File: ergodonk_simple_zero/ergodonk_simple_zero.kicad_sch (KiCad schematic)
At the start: 146 parts, among them J2 4PIN, Q1 TIP120, SW0 SW_PUSH_LED, SW08_RH10 SW_PUSH_LED, SW1 SW_PUSH_LED, SW10 SW_PUSH_LED, SW11 SW_PUSH_LED, SW12 SW_PUSH_LED, SW13 SW_PUSH_LED, SW14 SW_PUSH_LED, SW15 SW_PUSH_LED, SW16 SW_PUSH_LED, SW17 SW_PUSH_LED, SW18_RH10 SW_PUSH_LED, SW2 SW_PUSH_LED, SW20 SW_PUSH_LED, SW21 SW_PUSH_LED, SW22 SW_PUSH_LED, SW23 SW_PUSH_LED, SW24 SW_PUSH_LED, SW25 SW_PUSH_LED, SW26 SW_PUSH_LED, SW27 SW_PUSH_LED, SW28_RH10 SW_PUSH_LED, SW3 SW_PUSH_LED, SW30 SW_PUSH_LED, SW31 SW_PUSH_LED, SW32 SW_PUSH_LED, SW33 SW_PUSH_LED, SW34 SW_PUSH_LED, SW35 SW_PUSH_LED, SW36 SW_PUSH_LED, SW37 SW_PUSH_LED, SW38_RH10 SW_PUSH_LED, SW4 SW_PUSH_LED, SW40 SW_PUSH_LED, SW42 SW_PUSH_LED, SW43 SW_PUSH_LED, SW44 SW_PUSH_LED, SW45 SW_PUSH_LED, SW46 SW_PUSH_LED, SW47 SW_PUSH_LED, SW48_RH10 SW_PUSH_LED, SW5 SW_PUSH_LED, SW50 SW_PUSH_LED, SW51 SW_PUSH_LED, SW52 SW_PUSH_LED, SW53 SW_PUSH_LED, SW54 SW_PUSH_LED, SW55 SW_PUSH_LED, SW56 SW_PUSH_LED, SW57 SW_PUSH_LED, SW58 SW_PUSH_LED, SW6 SW_PUSH_LED, SW7 SW_PUSH_LED

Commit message: ergodonk simple zero checkpoint before choc MX switch swap
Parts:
- D_SOL_1: footprint ergodonk_simple:MUR340S_IN4001_TH_HYBRID -> Ergodonk_simple_zero:MUR340S_IN4001_TH_HYBRID
- H1, H10, H2, H3, H4, H5, H6, H7, H8, H9: footprint ergodonk_simple:Hole from sofle for M2 posts gold rimmer -> Ergodonk_simple_zero:Hole from sofle for M2 posts gold rimmer
- H11, H12, H13, H14, H15, H16, H17, H18, H19, H20, H21, H22, H23, H24, H25: footprint ergodonk_simple:M2_Hole_fancy_for_bolt-on-plate -> Ergodonk_simple_zero:M2_Hole_fancy_for_bolt-on-plate
- Q1: footprint ergodonk_simple:TO-220-3_Horizontal_TabDown -> Ergodonk_simple_zero:TO-220-3_Horizontal_TabDown
- SW0, SW1, SW10, SW11, SW12, SW13, SW14, SW16, SW17, SW2, SW20, SW21, SW22, SW23, SW24, SW25, SW26, SW3, SW30, SW31, SW32, SW33, SW34, SW35, SW36, SW4, SW40, SW42, SW43, SW44, SW45, SW46, SW5, SW50, SW51, SW52, SW53, SW54, SW55, SW56, SW57, SW58, SW6, SW7: footprint ergodonk_simple:Cherry_MX_DS_Hotswap_1U_sofle3b v3 -> Ergodonk_simple_zero:Cherry_MX_DS_Hotswap_1U_sofle3b v3
- SW08_RH10: footprint ergodonk_simple:V2_CherryMX_DoubleSided_Hotswap_miniE_2u_RH_ONLY -> Ergodonk_simple_zero:V2_CherryMX_DoubleSided_Hotswap_miniE_2u_RH_ONLY
- SW15: footprint kbd:CherryMX_Choc_Hotswap -> Ergodonk_simple_zero:CherryMX_Choc_Hotswap_ergodonk_simple_zero_56
- SW18_RH10, SW38_RH10: footprint ergodonk_simple:Cherry_MX_DS_Hotswap_1U_oneside -> Ergodonk_simple_zero:Cherry_MX_DS_Hotswap_1U_oneside
- SW27: footprint ergodonk_simple:V2_CherryMX_DoubleSided_Hotswap_miniE_1.5u_LH_1u_RH -> Ergodonk_simple_zero:V2_CherryMX_DoubleSided_Hotswap_miniE_1.5u_LH_1u_RH
- SW28_RH10: footprint ergodonk_simple:V2_CherryMX_DoubleSided_Hotswap_miniE_1.5u_RH_ONLY -> Ergodonk_simple_zero:V2_CherryMX_DoubleSided_Hotswap_miniE_1.5u_RH_ONLY
- SW37: footprint ergodonk_simple:V2_CherryMX_DoubleSided_Hotswap_miniE_1.75u_LH_1u_RH -> Ergodonk_simple_zero:V2_CherryMX_DoubleSided_Hotswap_miniE_1.75u_LH_1u_RH
- SW47: footprint ergodonk_simple:V2_CherryMX_DoubleSided_Hotswap_miniE_2.25u_LH_2.75u_RH -> Ergodonk_simple_zero:V2_CherryMX_DoubleSided_Hotswap_miniE_2.25u_LH_2.75u_RH
- SW48_RH10: footprint ergodonk_simple:V2_CherryMX_DoubleSided_Hotswap_miniE_2.25u_RH_ONLY -> Ergodonk_simple_zero:V2_CherryMX_DoubleSided_Hotswap_miniE_2.25u_RH_ONLY
- SWLH_ROT1: footprint ergodonk_simple:RotaryEncoder_EC11_ergodonk_variant -> Ergodonk_simple_zero:RotaryEncoder_EC11_ergodonk_variant

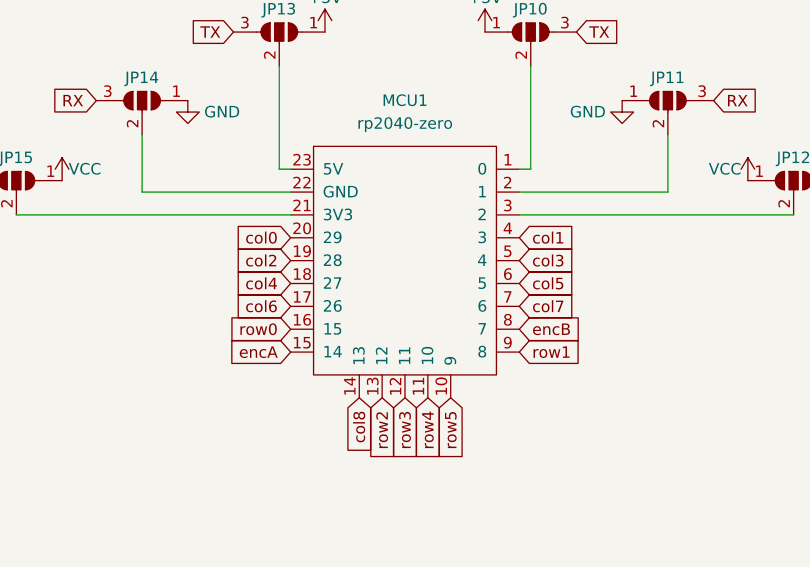
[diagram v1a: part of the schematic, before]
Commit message: Added choc support for ergodonk simple zero
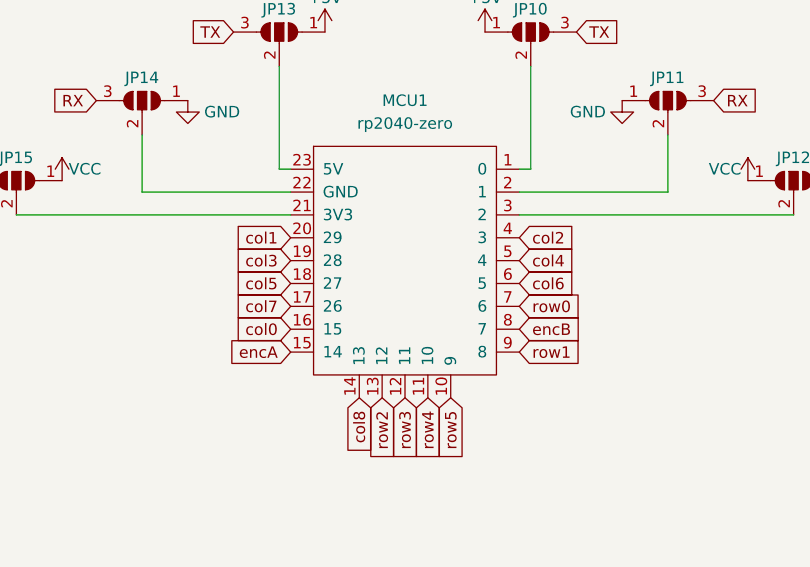
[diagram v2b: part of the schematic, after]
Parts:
- SW0, SW1, SW10, SW11, SW12, SW13, SW14, SW16, SW17, SW2, SW20, SW21, SW22, SW23, SW24, SW25, SW26, SW3, SW30, SW31, SW32, SW33, SW34, SW35, SW36, SW4, SW40, SW42, SW43, SW44, SW45, SW46, SW5, SW50, SW51, SW52, SW53, SW54, SW55, SW56, SW57, SW58, SW6, SW7: footprint Ergodonk_simple_zero:Cherry_MX_DS_Hotswap_1U_sofle3b v3 -> Ergodonk_simple_zero:CherryMX_Choc_Hotswap_ergodonk_simple_zero_56
- SW08_RH10: footprint Ergodonk_simple_zero:V2_CherryMX_DoubleSided_Hotswap_miniE_2u_RH_ONLY -> Ergodonk_simple_zero:CherryMX_Choc_Hotswap_ergodonk_simple_zero_SS_2U
- SW18_RH10, SW38_RH10: footprint Ergodonk_simple_zero:Cherry_MX_DS_Hotswap_1U_oneside -> Ergodonk_simple_zero:CherryMX_Choc_Hotswap_ergodonk_simple_zero_SS
- SW27: footprint Ergodonk_simple_zero:V2_CherryMX_DoubleSided_Hotswap_miniE_1.5u_LH_1u_RH -> Ergodonk_simple_zero:CherryMX_Choc_Hotswap_ergodonk_simple_zero_SS_1.5uLH_1uRH
- SW28_RH10: footprint Ergodonk_simple_zero:V2_CherryMX_DoubleSided_Hotswap_miniE_1.5u_RH_ONLY -> Ergodonk_simple_zero:CherryMX_Choc_Hotswap_ergodonk_simple_zero_SS_1.5U
- SW37: footprint Ergodonk_simple_zero:V2_CherryMX_DoubleSided_Hotswap_miniE_1.75u_LH_1u_RH -> Ergodonk_simple_zero:CherryMX_Choc_Hotswap_ergodonk_simple_zero_SS_1.75uLH_1uRH
- SW47: footprint Ergodonk_simple_zero:V2_CherryMX_DoubleSided_Hotswap_miniE_2.25u_LH_2.75u_RH -> Ergodonk_simple_zero:CherryMX_Choc_Hotswap_ergodonk_simple_zero_SS_2.25uLH 2.75uRH
- SW48_RH10: footprint Ergodonk_simple_zero:V2_CherryMX_DoubleSided_Hotswap_miniE_2.25u_RH_ONLY -> Ergodonk_simple_zero:CherryMX_Choc_Hotswap_ergodonk_simple_zero_SS_2.25U
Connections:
- net SW41A: now also MCU1.20 (29); no longer MCU1.4 (3)
- net col0: now also MCU1.16 (15); no longer MCU1.20 (29)
- net col2: now also MCU1.4 (3); no longer MCU1.19 (28)
- net col3: now also MCU1.19 (28); no longer MCU1.5 (4)
- net col4: now also MCU1.5 (4); no longer MCU1.18 (27)
- net col5: now also MCU1.18 (27); no longer MCU1.6 (5)
- net col6: now also MCU1.6 (5); no longer MCU1.17 (26)
- net col7: now also MCU1.17 (26); no longer MCU1.7 (6)
- net row0: now also MCU1.7 (6); no longer MCU1.16 (15)

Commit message: Most routing complete
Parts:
- D0, D08_RH10, D1, D10, D11, D12, D13, D14, D15, D16, D17, D18_RH10, D2, D20, D21, D22, D23, D24, D25, D26, D27, D28_RH10, D3, D30, D31, D32, D33, D34, D35, D36, D37, D38_RH10, D4, D40, D41, D42, D43, D44, D45, D46, D47, D48_RH10, D5, D50, D51, D52, D53, D54, D55, D56, D57, D58, D6, D7: footprint ergodonk_kicad_library:D_SOD-123_DO-35_Hybrid_DoubleSided -> Ergodonk_simple_zero:D_SOD-123_DO-35_Hybrid_DoubleSided_ergodonk_simple_zero
